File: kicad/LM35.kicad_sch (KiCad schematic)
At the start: 8 parts, among them J10 Screw_Terminal_01x05, U7 LM35-LP, U8 AH3712Q-P-B

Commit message: replace NAU7802SGI with NAU7802KGI i accidentally bought
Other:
- company: Dirty South Supercomputing -> dirty south supercomputing
- title: Dankdryer -> dankdryer
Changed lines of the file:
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@@
 	(paper "USLetter")
 	(title_block
-		(title "Dankdryer")
-		(date "2025-01-02")
-		(rev "1.0.1")
-		(company "Dirty South Supercomputing")
+		(title "dankdryer")
+		(date "2025-01-05")
+		(rev "1.1.0")
+		(company "dirty south supercomputing")
 		(comment 1 "nick black")
 	)

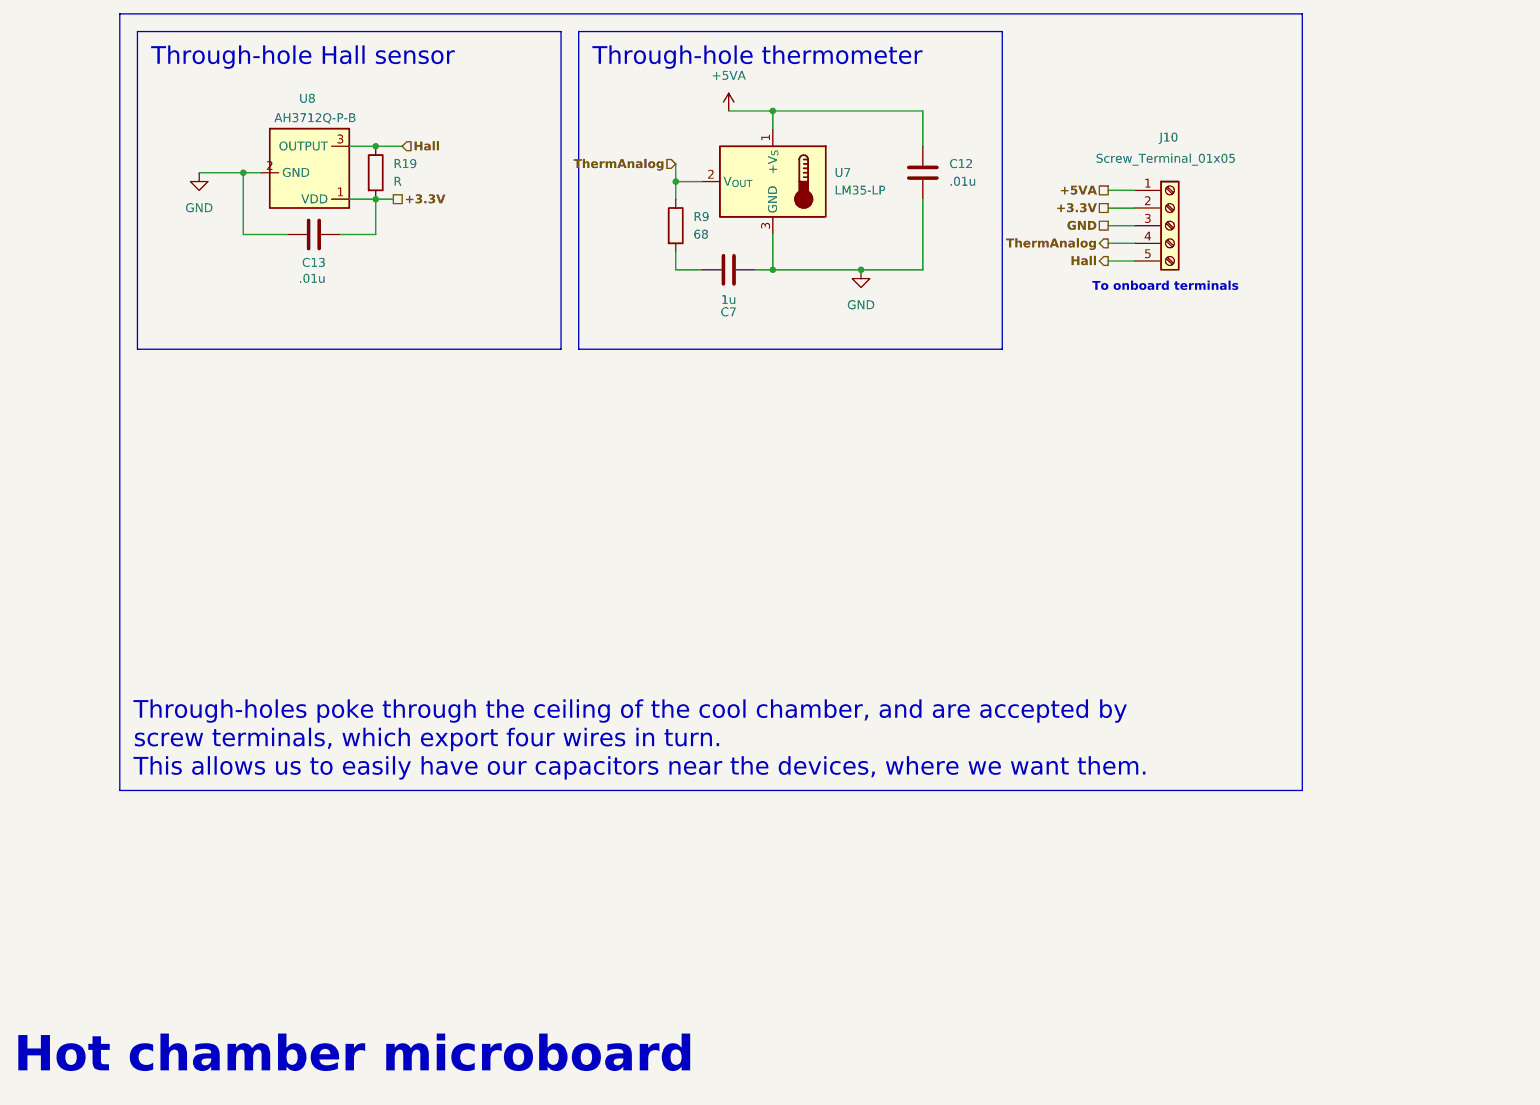
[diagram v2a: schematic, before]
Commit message: beefier capacitors on the microboard
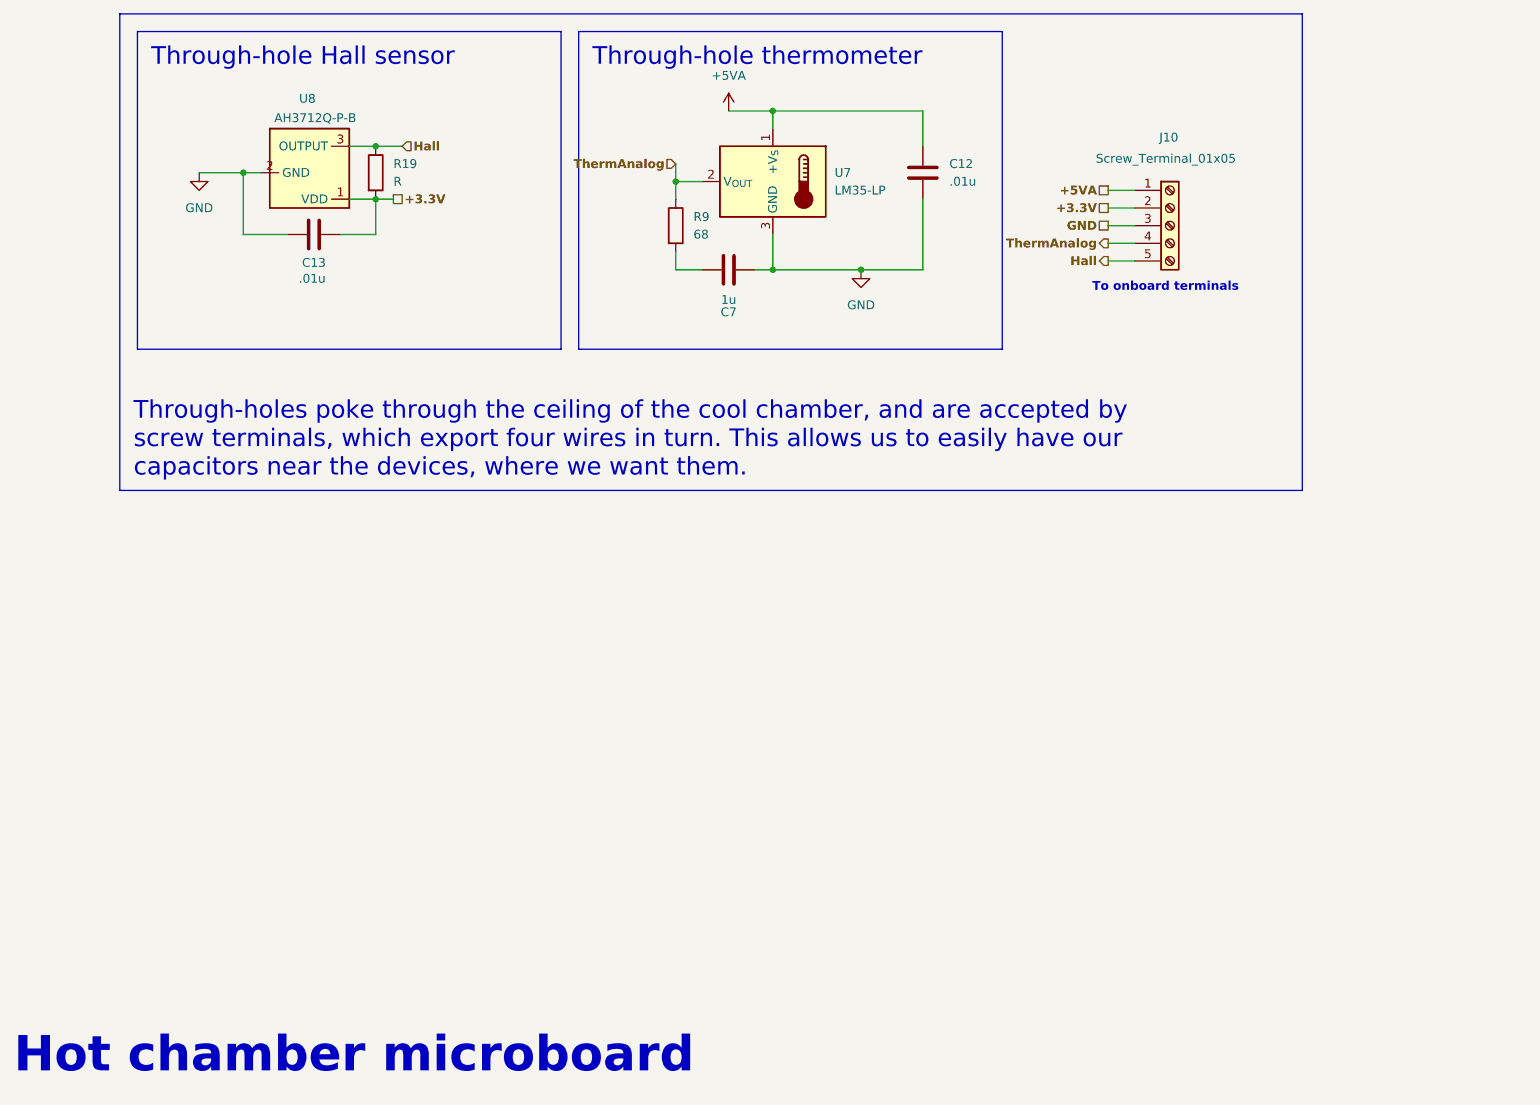
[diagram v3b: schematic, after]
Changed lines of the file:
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@@
 	(title_block
 		(title "dankdryer")
-		(date "2025-01-05")
-		(rev "1.1.0")
+		(date "2025-01-09")
+		(rev "1.2.0")
 		(company "dirty south supercomputing")
 		(comment 1 "nick black")
@@
 		)
 	)
-	(text_box "Through-holes poke through the ceiling of the cool chamber, and are accepted by screw terminals, which export four wires in turn.\nThis allows us to easily have our capacitors near the devices, where we want them."
+	(text_box "Through-holes poke through the ceiling of the cool chamber, and are accepted by screw terminals, which export four wires in turn. This allows us to easily have our capacitors near the devices, where we want them."
 		(exclude_from_sim no)
 		(at 45.72 38.1 0)
-		(size 170.18 111.76)
-		(stroke
-			(width 0)
+		(size 170.18 68.58)
+		(stroke
+			(width 0)
